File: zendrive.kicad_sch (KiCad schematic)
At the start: 43 parts, among them Q2 2N7000, Q3 2N7000, Q4 2N7000, SW1 SW_SPDT, U1 DG412xY, U2 OPA2134, U3 DG412xY, U4 DG412xY

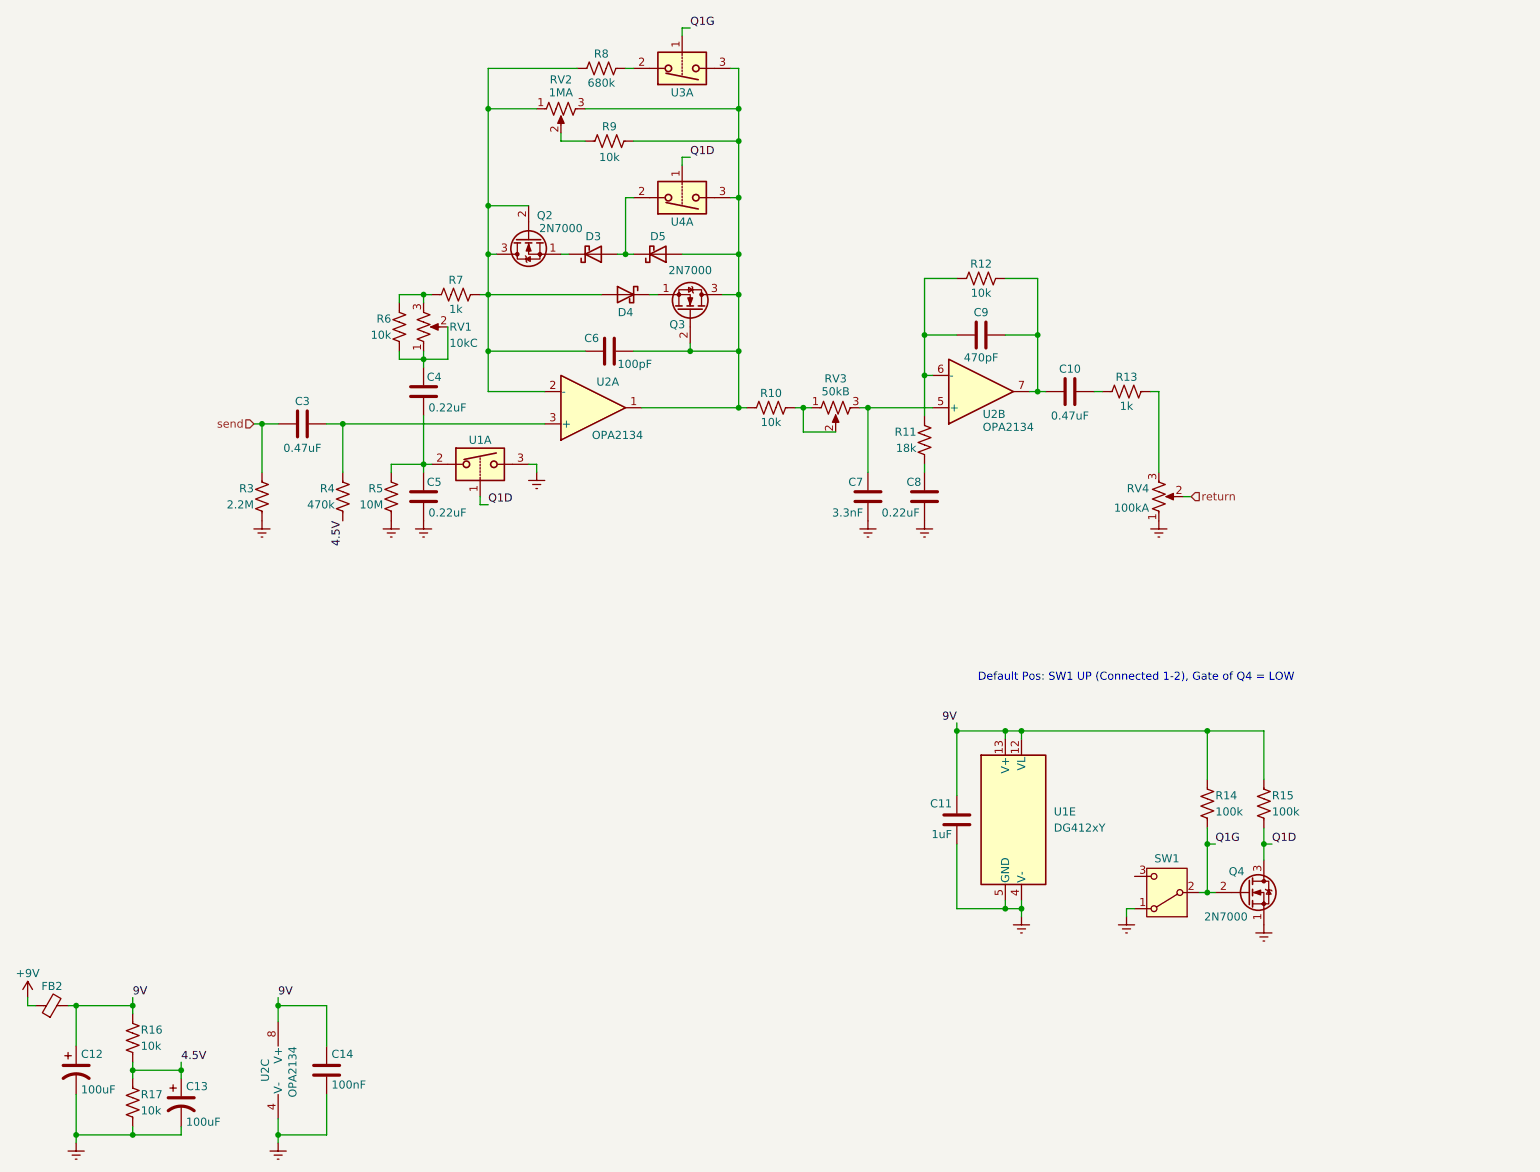
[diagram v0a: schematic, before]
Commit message: finished schematics, started PCB
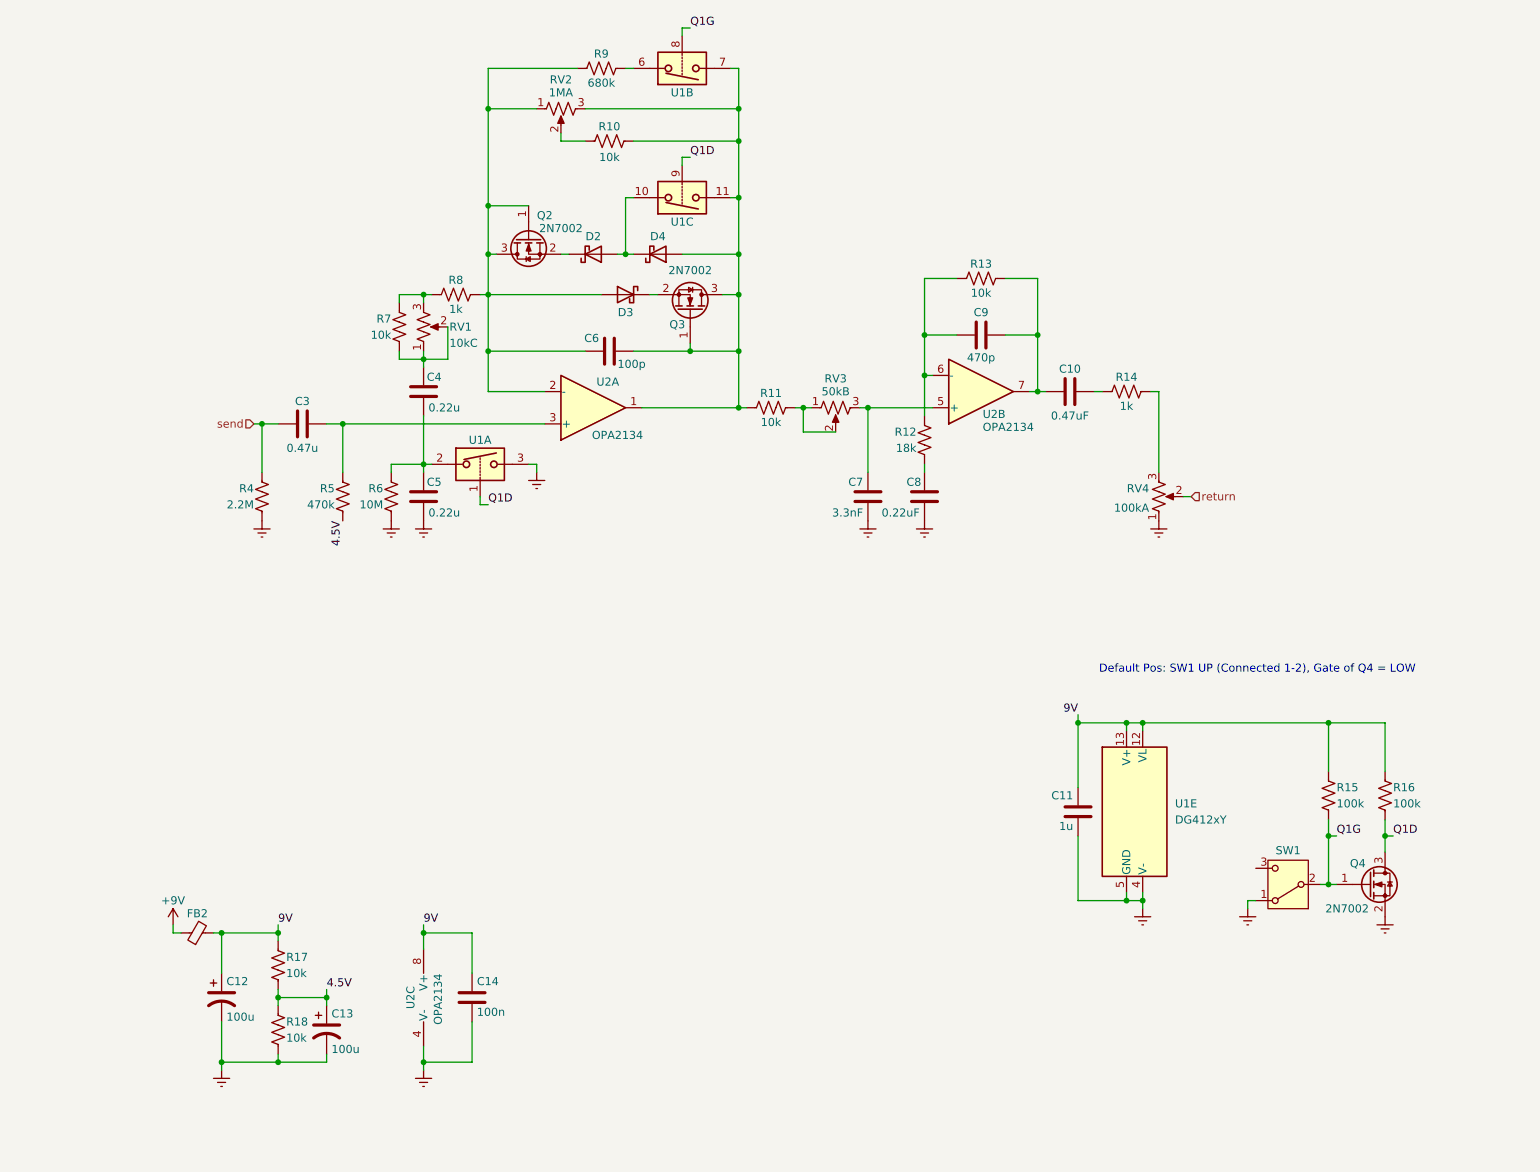
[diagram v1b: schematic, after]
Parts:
- C11: value 1uF -> 1u
- C12, C13: value 100uF -> 100u
- C14: value 100nF -> 100n
- C3: value 0.47uF -> 0.47u
- C4, C5: value 0.22uF -> 0.22u
- C6: value 100pF -> 100p; footprint bca-footprints:C_Ceramic_L4.0mm_W2.5mm_P2.50mm -> Capacitor_SMD:C_0805_2012Metric_Pad1.18x1.45mm_HandSolder
- C9: value 470pF -> 470p; footprint bca-footprints:C_Ceramic_L4.0mm_W2.5mm_P2.50mm -> Capacitor_SMD:C_0805_2012Metric_Pad1.18x1.45mm_HandSolder
- D2: renamed from D3; footprint bca-footprints:Diode_DO-35_P5.00mm -> Diode_SMD:D_SOD-323_HandSoldering
- D3: renamed from D4; footprint bca-footprints:Diode_DO-35_P5.00mm -> Diode_SMD:D_SOD-323_HandSoldering
- D4: renamed from D5; footprint bca-footprints:Diode_DO-35_P5.00mm -> Diode_SMD:D_SOD-323_HandSoldering
- Q2, Q3, Q4: value 2N7000 -> 2N7002; footprint bca-footprints:TO-92_Inline_Wide -> Package_TO_SOT_SMD:SOT-23_Handsoldering; symbol Transistor_FET:2N7000 -> Transistor_FET:2N7002
- R17: renamed from R16; footprint bca-footprints:R_L3.6mm_D1.6mm_P5.00mm_Horizontal -> Resistor_SMD:R_0805_2012Metric_Pad1.20x1.40mm_HandSolder
- R18: renamed from R17; footprint bca-footprints:R_L3.6mm_D1.6mm_P5.00mm_Horizontal -> Resistor_SMD:R_0805_2012Metric_Pad1.20x1.40mm_HandSolder
- renumbered R9 to R10, R10 to R11, R11 to R12, R12 to R13, R13 to R14, R14 to R15, R15 to R16, R3 to R4, R4 to R5, R5 to R6, R6 to R7, R7 to R8, R8 to R9, U3 to U1, U4 to U1
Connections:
- net Earth: now also Q4.2 (S); no longer Q4.1 (S)
- net Q1D: now also U1.9; no longer U1.1
- net Q1G: now also Q4.1 (G), U1.8; no longer Q4.2 (G), U1.1
- net at C6.2, D4.2 (A), Q3.3 (D)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: now also Q3.1 (G), U1.11, U1.7; no longer Q3.2 (G), U1.3, U1.3
- net at C6.1, D3.2 (A), Q2.3 (D)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: now also Q2.1 (G); no longer Q2.2 (G)
- net at D2.2 (A), D4.1 (K): now also U1.10; no longer U1.2
- net at R9.2: now also U1.6; no longer U1.2
- net at D3.1 (K): now also Q3.2 (S); no longer Q3.1 (S)
- net at D2.1 (K): now also Q2.2 (S); no longer Q2.1 (S)
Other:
- moved on the sheet: C11, C12, C13, C14, FB2, Q4, R15, R16, R17, R18, SW1, U1E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

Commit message: initial layout
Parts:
- C14, C6, C9: footprint Capacitor_SMD:C_0805_2012Metric_Pad1.18x1.45mm_HandSolder -> Capacitor_SMD:C_0603_1608Metric_Pad1.08x0.95mm_HandSolder
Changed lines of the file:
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@@
 			)
 		)
-		(property "Footprint" "Capacitor_SMD:C_0805_2012Metric_Pad1.18x1.45mm_HandSolder"
+		(property "Footprint" "Capacitor_SMD:C_0603_1608Metric_Pad1.08x0.95mm_HandSolder"
 			(at 176.53 65.0748 0)
 			(effects
@@
 			)
 		)
-		(property "Footprint" "Capacitor_SMD:C_0805_2012Metric_Pad1.18x1.45mm_HandSolder"
+		(property "Footprint" "Capacitor_SMD:C_0603_1608Metric_Pad1.08x0.95mm_HandSolder"
 			(at 118.11 67.6148 0)
 			(effects
@@
 			)
 		)
-		(property "Footprint" "Capacitor_SMD:C_0805_2012Metric_Pad1.18x1.45mm_HandSolder"
+		(property "Footprint" "Capacitor_SMD:C_0603_1608Metric_Pad1.08x0.95mm_HandSolder"
 			(at 93.6752 173.99 0)
 			(effects

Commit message: first draft PCB
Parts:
- D2, D3, D4: footprint Diode_SMD:D_SOD-323_HandSoldering -> bca-footprints:Diode_DO-35_P5.00mm
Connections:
- net Earth: now also U1.11; no longer U1.3
- net Q1D: now also U1.16; no longer U1.1
- net Q1G: now also U1.1; no longer U1.8
- net at C4.1, C5.2, R6.2: now also U1.10; no longer U1.2
- net at C6.2, D4.2 (A), Q3.1 (G)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: now also U1.14, U1.3; no longer U1.11, U1.7
- net at D2.2 (A), D4.1 (K): now also U1.15; no longer U1.10
- net at R9.2: now also U1.2; no longer U1.6
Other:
- moved on the sheet: U1A, U1C, U1D
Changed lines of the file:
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@@
 			)
 		)
-		(property "Footprint" "Diode_SMD:D_SOD-323_HandSoldering"
+		(property "Footprint" "bca-footprints:Diode_DO-35_P5.00mm"
 			(at 121.92 53.34 0)
 			(effects
@@
 	(symbol
 		(lib_id "Analog_Switch:DG412xY")
-		(at 125.73 24.13 0)
+		(at 125.73 44.45 0)
 		(mirror x)
-		(unit 2)
+		(unit 4)
 		(exclude_from_sim no)
 		(in_bom yes)
@@
 		(dnp no)
 		(property "Reference" "U1"
-			(at 125.73 27.94 0)
+			(at 125.73 48.26 0)
 			(effects
 				(font
@@
 		)
 		(property "Value" "DG412xY"
-			(at 124.4601 27.94 90)
+			(at 124.4601 48.26 90)
 			(effects
 				(font
@@
 		)
 		(property "Footprint" "Package_SO:SOIC-16_3.9x9.9mm_P1.27mm"
-			(at 125.73 21.59 0)
+			(at 125.73 41.91 0)
 			(effects
 				(font
@@
 		)
 		(property "Datasheet" "https://datasheets.maximintegrated.com/en/ds/DG411-DG413.pdf"
-			(at 125.73 24.13 0)
+			(at 125.73 44.45 0)
 			(effects
 				(font
@@
 		)
 		(property "Description" "Quad SPST Monolithic CMOS Analog Switches, normally OFF, 17Ohm Ron, SOIC-16"
-			(at 125.73 24.13 0)
+			(at 125.73 44.45 0)
 			(effects
 				(font
@@
 				(path "/0931d4cd-bc79-4e0b-a395-63d6dc93deda/04ae03a0-136b-4c60-aed5-23a9e7c56e8c"
 					(reference "U1")
-					(unit 2)
+					(unit 4)
 				)
 			)
@@
 	(symbol
 		(lib_id "Analog_Switch:DG412xY")
-		(at 125.73 44.45 0)
-		(mirror x)
+		(at 93.98 86.36 0)
 		(unit 3)
 		(exclude_from_sim no)
@@
 		(dnp no)
 		(property "Reference" "U1"
-			(at 125.73 48.26 0)
+			(at 93.98 82.55 0)
 			(effects
 				(font
@@
 		)
 		(property "Value" "DG412xY"
-			(at 124.4601 48.26 90)
+			(at 92.7101 82.55 90)
 			(effects
 				(font
@@
 		)
 		(property "Footprint" "Package_SO:SOIC-16_3.9x9.9mm_P1.27mm"
-			(at 125.73 41.91 0)
+			(at 93.98 88.9 0)
 			(effects
 				(font
@@
 		)
 		(property "Datasheet" "https://datasheets.maximintegrated.com/en/ds/DG411-DG413.pdf"
-			(at 125.73 44.45 0)
+			(at 93.98 86.36 0)
 			(effects
 				(font
@@
 		)
 		(property "Description" "Quad SPST Monolithic CMOS Analog Switches, normally OFF, 17Ohm Ron, SOIC-16"
-			(at 125.73 44.45 0)
+			(at 93.98 86.36 0)
 			(effects
 				(font
@@
 			)
 		)
-		(property "Footprint" "Diode_SMD:D_SOD-323_HandSoldering"
+		(property "Footprint" "bca-footprints:Diode_DO-35_P5.00mm"
 			(at 116.84 59.69 0)
 			(effects
@@
 			)
 		)
-		(property "Footprint" "Diode_SMD:D_SOD-323_HandSoldering"
+		(property "Footprint" "bca-footprints:Diode_DO-35_P5.00mm"
 			(at 111.76 53.34 0)
 			(effects
@@
 	(symbol
 		(lib_id "Analog_Switch:DG412xY")
-		(at 93.98 86.36 0)
+		(at 125.73 24.13 0)
+		(mirror x)
 		(unit 1)
 		(exclude_from_sim no)
@@
 		(dnp no)
 		(property "Reference" "U1"
-			(at 93.98 82.55 0)
+			(at 125.73 27.94 0)
 			(effects
 				(font
@@
 		)
 		(property "Value" "DG412xY"
-			(at 92.7101 82.55 90)
+			(at 124.4601 27.94 90)
 			(effects
 				(font
@@
 		)
 		(property "Footprint" "Package_SO:SOIC-16_3.9x9.9mm_P1.27mm"
-			(at 93.98 88.9 0)
+			(at 125.73 21.59 0)
 			(effects
 				(font
@@
 		)
 		(property "Datasheet" "https://datasheets.maximintegrated.com/en/ds/DG411-DG413.pdf"
-			(at 93.98 86.36 0)
+			(at 125.73 24.13 0)
 			(effects
 				(font
@@
 		)
 		(property "Description" "Quad SPST Monolithic CMOS Analog Switches, normally OFF, 17Ohm Ron, SOIC-16"
-			(at 93.98 86.36 0)
+			(at 125.73 24.13 0)
 			(effects
 				(font

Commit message: generated production files
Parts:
- C11: value 1u -> 1uF
- C12, C13: value 100u -> 100uF
- C14: value 100n -> 100nF
- C3: value 0.47u -> 0.47uF
- C4, C5: value 0.22u -> 0.22uF
- C6: value 100p -> 100pF
- C9: value 470p -> 470pF
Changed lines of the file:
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@@
 			)
 		)
-		(property "Value" "0.22u"
+		(property "Value" "0.22uF"
 			(at 85.852 77.47 0)
 			(effects
@@
 			)
 		)
-		(property "Value" "470p"
+		(property "Value" "470pF"
 			(at 172.72 69.596 90)
 			(effects
@@
 			)
 		)
-		(property "Value" "0.47u"
+		(property "Value" "0.47uF"
 			(at 66.04 83.82 90)
 			(effects
@@
 			)
 		)
-		(property "Value" "100u"
+		(property "Value" "100uF"
 			(at 54.102 173.228 0)
 			(effects
@@
 			)
 		)
-		(property "Value" "0.22u"
+		(property "Value" "0.22uF"
 			(at 85.852 93.98 0)
 			(effects
@@
 			)
 		)
-		(property "Value" "100p"
+		(property "Value" "100pF"
 			(at 115.57 70.612 90)
 			(effects
@@
 			)
 		)
-		(property "Value" "100n"
+		(property "Value" "100nF"
 			(at 93.472 172.466 0)
 			(effects
@@
 			)
 		)
-		(property "Value" "1u"
+		(property "Value" "1uF"
 			(at 187.198 143.256 0)
 			(effects
@@
 			)
 		)
-		(property "Value" "100u"
+		(property "Value" "100uF"
 			(at 70.612 178.308 0)
 			(effects
